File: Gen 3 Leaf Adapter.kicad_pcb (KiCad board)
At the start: 4 copper layers, 131.6 x 103.3 mm, 95 parts, among them J1 Conn_02x16_Top_Bottom_Mountin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, J2 Conn_02x20_Top_Bottom_Mountin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, J3 Conn_02x05_Odd_Even, J4 Conn_01x06_Male, J8 Conn_01x03_Male, Q1 Q_NMOS_GDS, Q2 Q_NMOS_GDS, Q3 IRLML0100TRPBF, Q4 IRLML0100TRPBF, Q5 IRLML0100TRPBF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

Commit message: V0.0.2
Removed R17, corrected throttle voltages from 0-3.3 to 0-6.6v, corrected schematic notes, mini mainboard symbol (V2), updated silkscreen to V0.0.2, and added a 2nd page to the schematic to track revision changes.
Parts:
- removed R17: 10K, Resistor_SMD:R_0805_2012Metric_Pad1.20x1.40mm_HandSolder
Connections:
- J2 pad 40: Net-(J2-Pad40) -> SIG_EMCYSTOP
- SJ5 pad 2: Net-(J2-Pad40) -> SIG_EMCYSTOP
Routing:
- net SIG_EMCYSTOP: track 66.3 -> 99.8 mm, vias 1 -> 3
- net Net-(J2-Pad40): track 29.9 -> 0.00 mm, vias 2 -> 0
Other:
- board text added: "Gen. 3 Leaf Mini Mainboard Adapter V0.0.2"
- board text removed: "Gen. 3 Leaf Mini Mainboard Adapter V0.0.1"

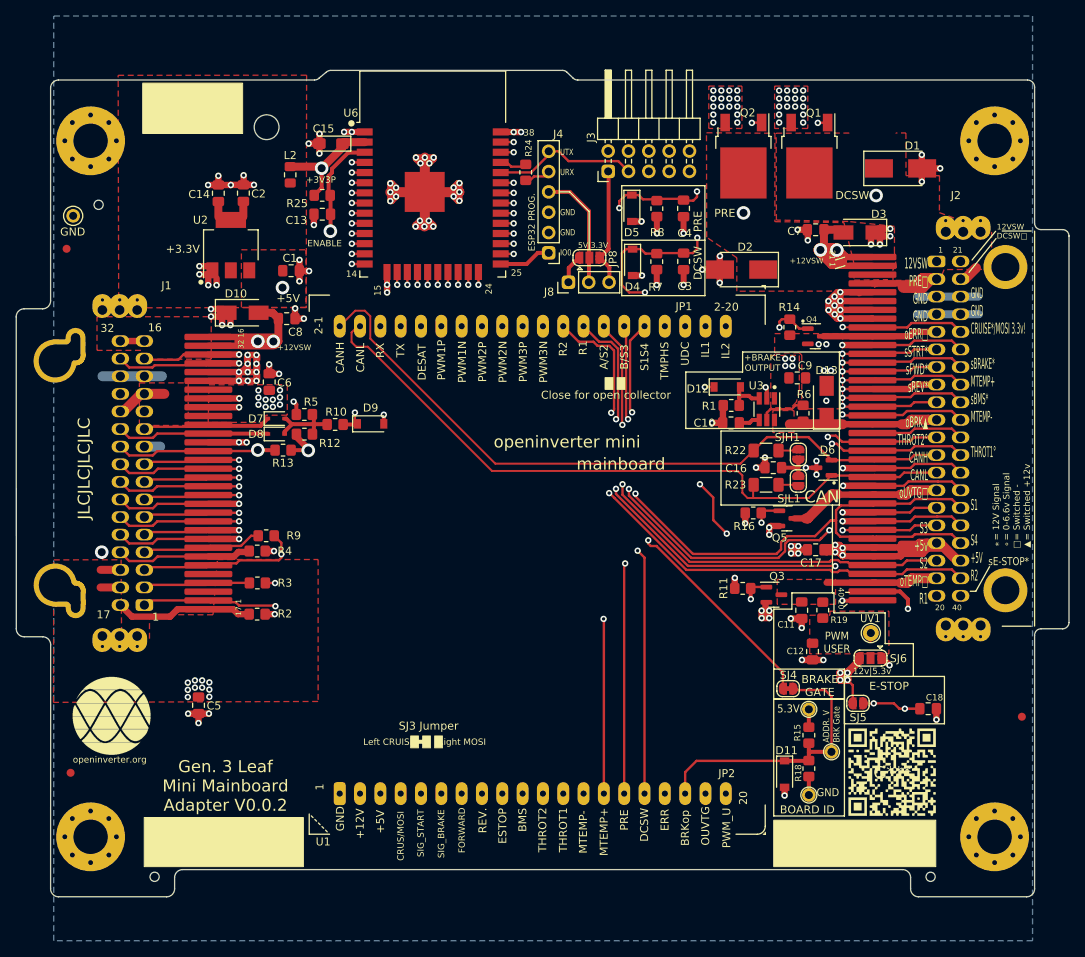
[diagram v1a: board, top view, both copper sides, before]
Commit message: V0.0.3 update
Corrected L2 inductor to one properly sized.  From 0805 to a Sunlord 4030 / 4.0mmX4.0mm inductor.
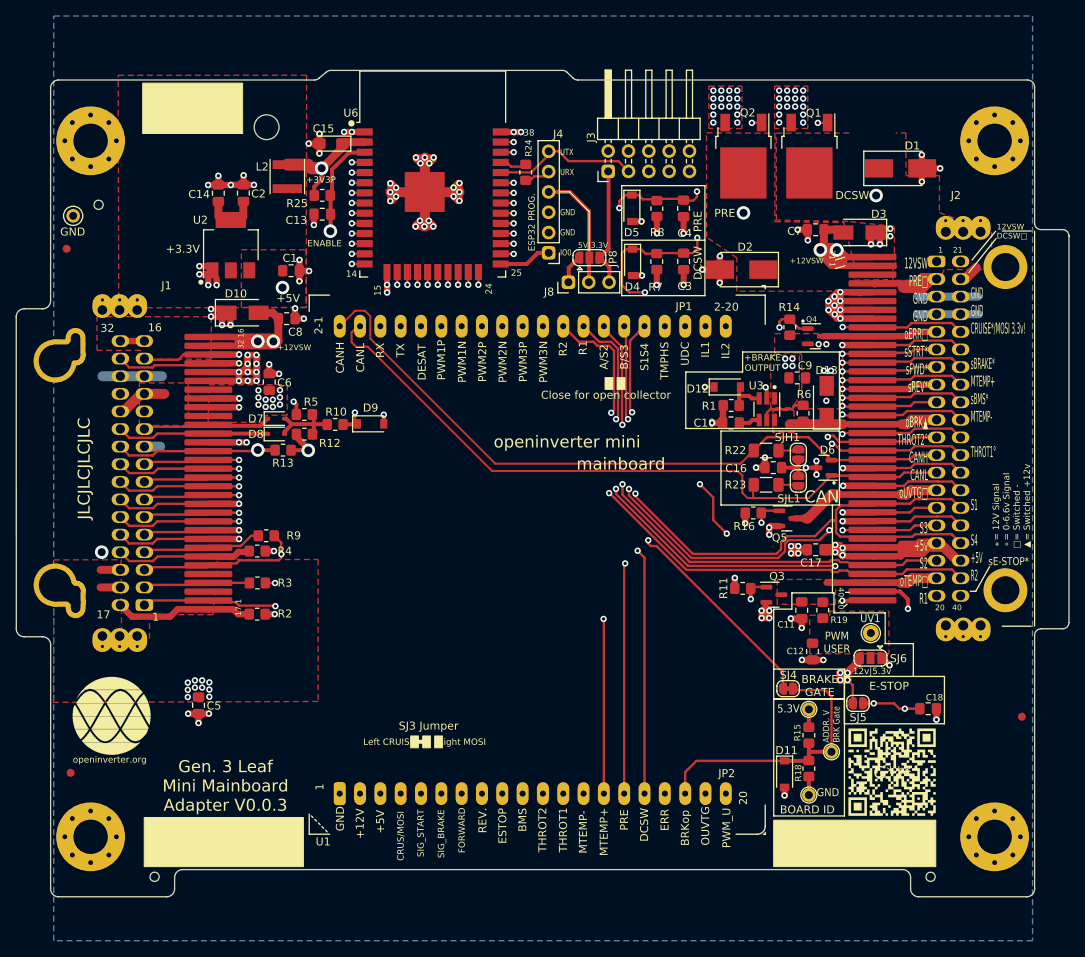
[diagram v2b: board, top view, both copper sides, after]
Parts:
- L2: value 10uH 1.15OHM -> 10uH; footprint Inductor_SMD:L_0805_2012Metric_Pad1.15x1.40mm_HandSolder -> OpenInverter Library:Inductor_Sunlord_4030
- moved L2 0.43 mm to (104.6, 54.5)
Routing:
- net unconnected-(J2-Pad31): track 11.9 -> 15.8 mm, vias 0 -> 1
- net +3.3VP: track 73.2 -> 73.9 mm
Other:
- board text added: "Gen. 3 Leaf Mini Mainboard Adapter V0.0.3"
- board text removed: "Gen. 3 Leaf Mini Mainboard Adapter V0.0.2"
